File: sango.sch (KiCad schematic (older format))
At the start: 12 parts

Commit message: add high-side driver pFET
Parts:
- added Q?: NTR2101P, Package_TO_SOT_SMD:SOT-23, symbol Transistor_FET:NTR2101P
- added R?: 10k, symbol Device:R
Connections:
- net +5V: now also Q?.2 (S), R?.2
- net at U?.10 (3.0_IND#): now also U?.9 (1.5_IND#), Q?.1 (G), R?.1
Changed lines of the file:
@@
 	1    0    0    -1
 $EndComp
+$Comp
+L Transistor_FET:NTR2101P Q?
+U 1 1 5BE8FFD4
+P 8400 2000
+F 0 "Q?" V 8743 2000 50  0000 C CNN
+F 1 "NTR2101P" V 8652 2000 50  0000 C CNN
+F 2 "Package_TO_SOT_SMD:SOT-23" H 8600 1925 50  0001 L CIN
+F 3 "http://www.onsemi.com/pub/Collateral/NTR2101P-D.PDF" H 8400 2000 50  0001 L CNN
+	1    8400 2000
+	0    1    -1   0
+$EndComp
+Wire Wire Line
+	6800 3150 8400 3150
+Wire Wire Line
+	6800 3300 8400 3300
+Wire Wire Line
+	8400 3300 8400 3150
+Wire Wire Line
+	8400 3150 8400 2400
+Connection ~ 8400 3150
+Wire Wire Line
+	5900 1900 8100 1900
+Connection ~ 5900 1900
+$Comp
+L Device:R R?
+U 1 1 5BE95889
+P 8100 2150
+F 0 "R?" V 8180 2150 50  0000 C CNN
+F 1 "10k" V 8100 2150 50  0000 C CNN
+F 2 "" V 8030 2150 50  0001 C CNN
+F 3 "" H 8100 2150 50  0001 C CNN
+	1    8100 2150
+	-1   0    0    1
+$EndComp
+Wire Wire Line
+	8100 2000 8100 1900
+Connection ~ 8100 1900
+Wire Wire Line
+	8100 1900 8200 1900
+Wire Wire Line
+	8100 2300 8100 2400
+Wire Wire Line
+	8100 2400 8400 2400
+Connection ~ 8400 2400
+Wire Wire Line
+	8400 2400 8400 2200
 $EndSCHEMATC

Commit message: fix: OSC --> OCS typo
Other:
- note added: "TODO: button (to GND) as input to OCS#\nOSC# has a Schmitt-triggered input with a pull-up"
- note removed: "TODO: button (to GND) as input to OSC#\nOSC# has a Schmitt-triggered input with a pull-up"
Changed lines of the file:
@@
 Connection ~ 4350 5100
 Text Notes 4250 1250 0    60   ~ 0
-TODO: button (to GND) as input to OSC#\nOSC# has a Schmitt-triggered input with a pull-up
+TODO: button (to GND) as input to OCS#\nOSC# has a Schmitt-triggered input with a pull-up
 Wire Wire Line
 	4350 3150 4600 3150

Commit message: add Description field to UTC2000 schematic symbol
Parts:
- U?: Description (none) -> Basic USB Type-C Controller; Manufacturer Part Number (none) -> UTC2000-I/MG; ManufacturerPN UTC2000-I/MG -> (none); Supplier (none) -> Digi-Key; Supplier Part Number (none) -> UTC2000-I/MG-ND; Supplier1 Digi-Key -> (none); Supplier1PN UTC2000-I/MG-ND -> (none)
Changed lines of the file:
@@
 F 2 "" H 3900 3400 50  0001 C CIN
 F 3 "http://ww1.microchip.com/downloads/en/DeviceDoc/UTC2000%20DS%2000001957C.pdf" H 5900 2100 50  0001 C CNN
-F 4 "Microchip Technology" H 5900 2100 60  0001 C CNN "Manufacturer"
-F 5 "UTC2000-I/MG" H 5900 2100 60  0001 C CNN "ManufacturerPN"
-F 6 "Digi-Key" H 5900 2100 60  0001 C CNN "Supplier1"
-F 7 "UTC2000-I/MG-ND" H 5900 2100 60  0001 C CNN "Supplier1PN"
+F 4 "Basic USB Type-C Controller" H 5900 2100 60  0001 C CNN "Description"
+F 5 "Microchip Technology" H 5900 2100 60  0001 C CNN "Manufacturer"
+F 6 "UTC2000-I/MG" H 5900 2100 60  0001 C CNN "Manufacturer Part Number"
+F 7 "Digi-Key" H 5900 2100 60  0001 C CNN "Supplier"
+F 8 "UTC2000-I/MG-ND" H 5900 2100 60  0001 C CNN "Supplier Part Number"
 	1    5900 2850
 	1    0    0    -1

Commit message: fix: resistor value for voltage divider on VMON
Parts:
- R?: value 5.1k -> 35.7k
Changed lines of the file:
@@
 P 4200 2550
 F 0 "R?" V 4280 2550 50  0000 C CNN
-F 1 "5.1k" V 4200 2550 50  0000 C CNN
+F 1 "35.7k" V 4200 2550 50  0000 C CNN
 F 2 "" V 4130 2550 50  0001 C CNN
 F 3 "" H 4200 2550 50  0001 C CNN

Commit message: add part numbers for resistors and PFET
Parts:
- Q?: Description (none) -> MOSFET P-CH 8V 3.7A SOT-23; Manufacturer (none) -> ON Semiconductor; Manufacturer Part Number (none) -> NTR2101PT1G; Supplier (none) -> Digi-Key; Supplier Part Number (none) -> NTR2101PT1GOSCT-ND
- R? (x5): Description (none) -> RES SMD 10K OHM 1% 1/10W 0603; Manufacturer (none) -> Panasonic Electronic Components; Manufacturer Part Number (none) -> ERJ-3EKF1002V; Supplier (none) -> Digi-Key; Supplier Part Number (none) -> P10.0KHCT-ND
- R? (x3): Description (none) -> RES SMD 5.1K OHM 1% 1/10W 0603; Manufacturer (none) -> Panasonic Electronic Components; Manufacturer Part Number (none) -> ERJ-3EKF5101V; Supplier (none) -> Digi-Key; Supplier Part Number (none) -> P5.10KHCT-ND
- R?: Description (none) -> RES SMD 35.7K OHM 1% 1/10W 0603; Manufacturer (none) -> Panasonic Electronic Components; Manufacturer Part Number (none) -> ERJ-3EKF3572V; Supplier (none) -> Digi-Key; Supplier Part Number (none) -> P35.7KHCT-ND
- R?: Description (none) -> RES SMD 1M OHM 1% 1/10W 0603; Manufacturer (none) -> Panasonic Electronic Components; Manufacturer Part Number (none) -> ERJ-3EKF1004V; Supplier (none) -> Digi-Key; Supplier Part Number (none) -> P1.00MHCT-ND
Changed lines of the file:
@@
 F 1 "10k" V 4750 3150 50  0000 C CNN
 F 2 "" V 4680 3150 50  0001 C CNN
-F 3 "" H 4750 3150 50  0001 C CNN
+F 3 "https://industrial.panasonic.com/cdbs/www-data/pdf/RDA0000/AOA0000C304.pdf" H 4750 3150 50  0001 C CNN
+F 4 "RES SMD 10K OHM 1% 1/10W 0603" H 4750 3150 50  0001 C CNN "Description"
+F 5 "Panasonic Electronic Components" H 4750 3150 50  0001 C CNN "Manufacturer"
+F 6 "ERJ-3EKF1002V" H 4750 3150 50  0001 C CNN "Manufacturer Part Number"
+F 7 "Digi-Key" H 4750 3150 50  0001 C CNN "Supplier"
+F 8 "P10.0KHCT-ND" H 4750 3150 50  0001 C CNN "Supplier Part Number"
 	1    4750 3150
 	0    -1   -1   0
@@
 F 1 "10k" V 4750 3300 50  0000 C CNN
 F 2 "" V 4680 3300 50  0001 C CNN
-F 3 "" H 4750 3300 50  0001 C CNN
+F 3 "https://industrial.panasonic.com/cdbs/www-data/pdf/RDA0000/AOA0000C304.pdf" H 4750 3300 50  0001 C CNN
+F 4 "RES SMD 10K OHM 1% 1/10W 0603" H 4750 3300 50  0001 C CNN "Description"
+F 5 "Panasonic Electronic Components" H 4750 3300 50  0001 C CNN "Manufacturer"
+F 6 "ERJ-3EKF1002V" H 4750 3300 50  0001 C CNN "Manufacturer Part Number"
+F 7 "Digi-Key" H 4750 3300 50  0001 C CNN "Supplier"
+F 8 "P10.0KHCT-ND" H 4750 3300 50  0001 C CNN "Supplier Part Number"
 	1    4750 3300
 	0    1    1    0
@@
 F 1 "5.1k" V 4500 3550 50  0000 C CNN
 F 2 "" V 4430 3550 50  0001 C CNN
-F 3 "" H 4500 3550 50  0001 C CNN
+F 3 "https://industrial.panasonic.com/cdbs/www-data/pdf/RDA0000/AOA0000C304.pdf" H 4500 3550 50  0001 C CNN
+F 4 "RES SMD 5.1K OHM 1% 1/10W 0603" H 4500 3550 50  0001 C CNN "Description"
+F 5 "Panasonic Electronic Components" H 4500 3550 50  0001 C CNN "Manufacturer"
+F 6 "ERJ-3EKF5101V" H 4500 3550 50  0001 C CNN "Manufacturer Part Number"
+F 7 "Digi-Key" H 4500 3550 50  0001 C CNN "Supplier"
+F 8 "P5.10KHCT-ND" H 4500 3550 50  0001 C CNN "Supplier Part Number"
 	1    4500 3550
 	1    0    0    -1
@@
 F 1 "5.1k" V 4350 3550 50  0000 C CNN
 F 2 "" V 4280 3550 50  0001 C CNN
-F 3 "" H 4350 3550 50  0001 C CNN
+F 3 "https://industrial.panasonic.com/cdbs/www-data/pdf/RDA0000/AOA0000C304.pdf" H 4350 3550 50  0001 C CNN
+F 4 "RES SMD 5.1K OHM 1% 1/10W 0603" H 4350 3550 50  0001 C CNN "Description"
+F 5 "Panasonic Electronic Components" H 4350 3550 50  0001 C CNN "Manufacturer"
+F 6 "ERJ-3EKF5101V" H 4350 3550 50  0001 C CNN "Manufacturer Part Number"
+F 7 "Digi-Key" H 4350 3550 50  0001 C CNN "Supplier"
+F 8 "P5.10KHCT-ND" H 4350 3550 50  0001 C CNN "Supplier Part Number"
 	1    4350 3550
 	-1   0    0    1
@@
 F 1 "10k" V 4700 2150 50  0000 C CNN
 F 2 "" V 4630 2150 50  0001 C CNN
-F 3 "" H 4700 2150 50  0001 C CNN
+F 3 "https://industrial.panasonic.com/cdbs/www-data/pdf/RDA0000/AOA0000C304.pdf" H 4700 2150 50  0001 C CNN
+F 4 "RES SMD 10K OHM 1% 1/10W 0603" H 4700 2150 50  0001 C CNN "Description"
+F 5 "Panasonic Electronic Components" H 4700 2150 50  0001 C CNN "Manufacturer"
+F 6 "ERJ-3EKF1002V" H 4700 2150 50  0001 C CNN "Manufacturer Part Number"
+F 7 "Digi-Key" H 4700 2150 50  0001 C CNN "Supplier"
+F 8 "P10.0KHCT-ND" H 4700 2150 50  0001 C CNN "Supplier Part Number"
 	1    4700 2150
 	-1   0    0    1
@@
 F 1 "10k" V 4850 2150 50  0000 C CNN
 F 2 "" V 4780 2150 50  0001 C CNN
-F 3 "" H 4850 2150 50  0001 C CNN
+F 3 "https://industrial.panasonic.com/cdbs/www-data/pdf/RDA0000/AOA0000C304.pdf" H 4850 2150 50  0001 C CNN
+F 4 "RES SMD 10K OHM 1% 1/10W 0603" H 4850 2150 50  0001 C CNN "Description"
+F 5 "Panasonic Electronic Components" H 4850 2150 50  0001 C CNN "Manufacturer"
+F 6 "ERJ-3EKF1002V" H 4850 2150 50  0001 C CNN "Manufacturer Part Number"
+F 7 "Digi-Key" H 4850 2150 50  0001 C CNN "Supplier"
+F 8 "P10.0KHCT-ND" H 4850 2150 50  0001 C CNN "Supplier Part Number"
 	1    4850 2150
 	1    0    0    -1
@@
 F 1 "5.1k" V 4200 2950 50  0000 C CNN
 F 2 "" V 4130 2950 50  0001 C CNN
-F 3 "" H 4200 2950 50  0001 C CNN
+F 3 "https://industrial.panasonic.com/cdbs/www-data/pdf/RDA0000/AOA0000C304.pdf" H 4200 2950 50  0001 C CNN
+F 4 "RES SMD 5.1K OHM 1% 1/10W 0603" H 4200 2950 50  0001 C CNN "Description"
+F 5 "Panasonic Electronic Components" H 4200 2950 50  0001 C CNN "Manufacturer"
+F 6 "ERJ-3EKF5101V" H 4200 2950 50  0001 C CNN "Manufacturer Part Number"
+F 7 "Digi-Key" H 4200 2950 50  0001 C CNN "Supplier"
+F 8 "P5.10KHCT-ND" H 4200 2950 50  0001 C CNN "Supplier Part Number"
 	1    4200 2950
 	-1   0    0    1
@@
 F 1 "35.7k" V 4200 2550 50  0000 C CNN
 F 2 "" V 4130 2550 50  0001 C CNN
-F 3 "" H 4200 2550 50  0001 C CNN
+F 3 "https://industrial.panasonic.com/cdbs/www-data/pdf/RDA0000/AOA0000C304.pdf" H 4200 2550 50  0001 C CNN
+F 4 "RES SMD 35.7K OHM 1% 1/10W 0603" H 4200 2550 50  0001 C CNN "Description"
+F 5 "Panasonic Electronic Components" H 4200 2550 50  0001 C CNN "Manufacturer"
+F 6 "ERJ-3EKF3572V" H 4200 2550 50  0001 C CNN "Manufacturer Part Number"
+F 7 "Digi-Key" H 4200 2550 50  0001 C CNN "Supplier"
+F 8 "P35.7KHCT-ND" H 4200 2550 50  0001 C CNN "Supplier Part Number"
 	1    4200 2550
 	-1   0    0    1
@@
 F 1 "1M" V 2900 4850 50  0000 C CNN
 F 2 "" V 2830 4850 50  0001 C CNN
-F 3 "" H 2900 4850 50  0001 C CNN
+F 3 "https://industrial.panasonic.com/cdbs/www-data/pdf/RDA0000/AOA0000C304.pdf" H 2900 4850 50  0001 C CNN
+F 4 "RES SMD 1M OHM 1% 1/10W 0603" H 2900 4850 50  0001 C CNN "Description"
+F 5 "Panasonic Electronic Components" H 2900 4850 50  0001 C CNN "Manufacturer"
+F 6 "ERJ-3EKF1004V" H 2900 4850 50  0001 C CNN "Manufacturer Part Number"
+F 7 "Digi-Key" H 2900 4850 50  0001 C CNN "Supplier"
+F 8 "P1.00MHCT-ND" H 2900 4850 50  0001 C CNN "Supplier Part Number"
 	1    2900 4850
 	1    0    0    1
@@
 F 2 "Package_TO_SOT_SMD:SOT-23" H 8600 1925 50  0001 L CIN
 F 3 "http://www.onsemi.com/pub/Collateral/NTR2101P-D.PDF" H 8400 2000 50  0001 L CNN
+F 4 "MOSFET P-CH 8V 3.7A SOT-23" H 8400 2000 50  0001 L CNN "Description"
+F 5 "ON Semiconductor" H 8400 2000 50  0001 L CNN "Manufacturer"
+F 6 "NTR2101PT1G" H 8400 2000 50  0001 L CNN "Manufacturer Part Number"
+F 7 "Digi-Key" H 8400 2000 50  0001 L CNN "Supplier"
+F 8 "NTR2101PT1GOSCT-ND" H 8400 2000 50  0001 L CNN "Supplier Part Number"
 	1    8400 2000
 	0    1    -1   0
@@
 F 1 "10k" V 8100 2150 50  0000 C CNN
 F 2 "" V 8030 2150 50  0001 C CNN
-F 3 "" H 8100 2150 50  0001 C CNN
+F 3 "https://industrial.panasonic.com/cdbs/www-data/pdf/RDA0000/AOA0000C304.pdf" H 8100 2150 50  0001 C CNN
+F 4 "RES SMD 10K OHM 1% 1/10W 0603" H 8100 2150 50  0001 C CNN "Description"
+F 5 "Panasonic Electronic Components" H 8100 2150 50  0001 C CNN "Manufacturer"
+F 6 "ERJ-3EKF1002V" H 8100 2150 50  0001 C CNN "Manufacturer Part Number"
+F 7 "Digi-Key" H 8100 2150 50  0001 C CNN "Supplier"
+F 8 "P10.0KHCT-ND" H 8100 2150 50  0001 C CNN "Supplier Part Number"
 	1    8100 2150
 	-1   0    0    1

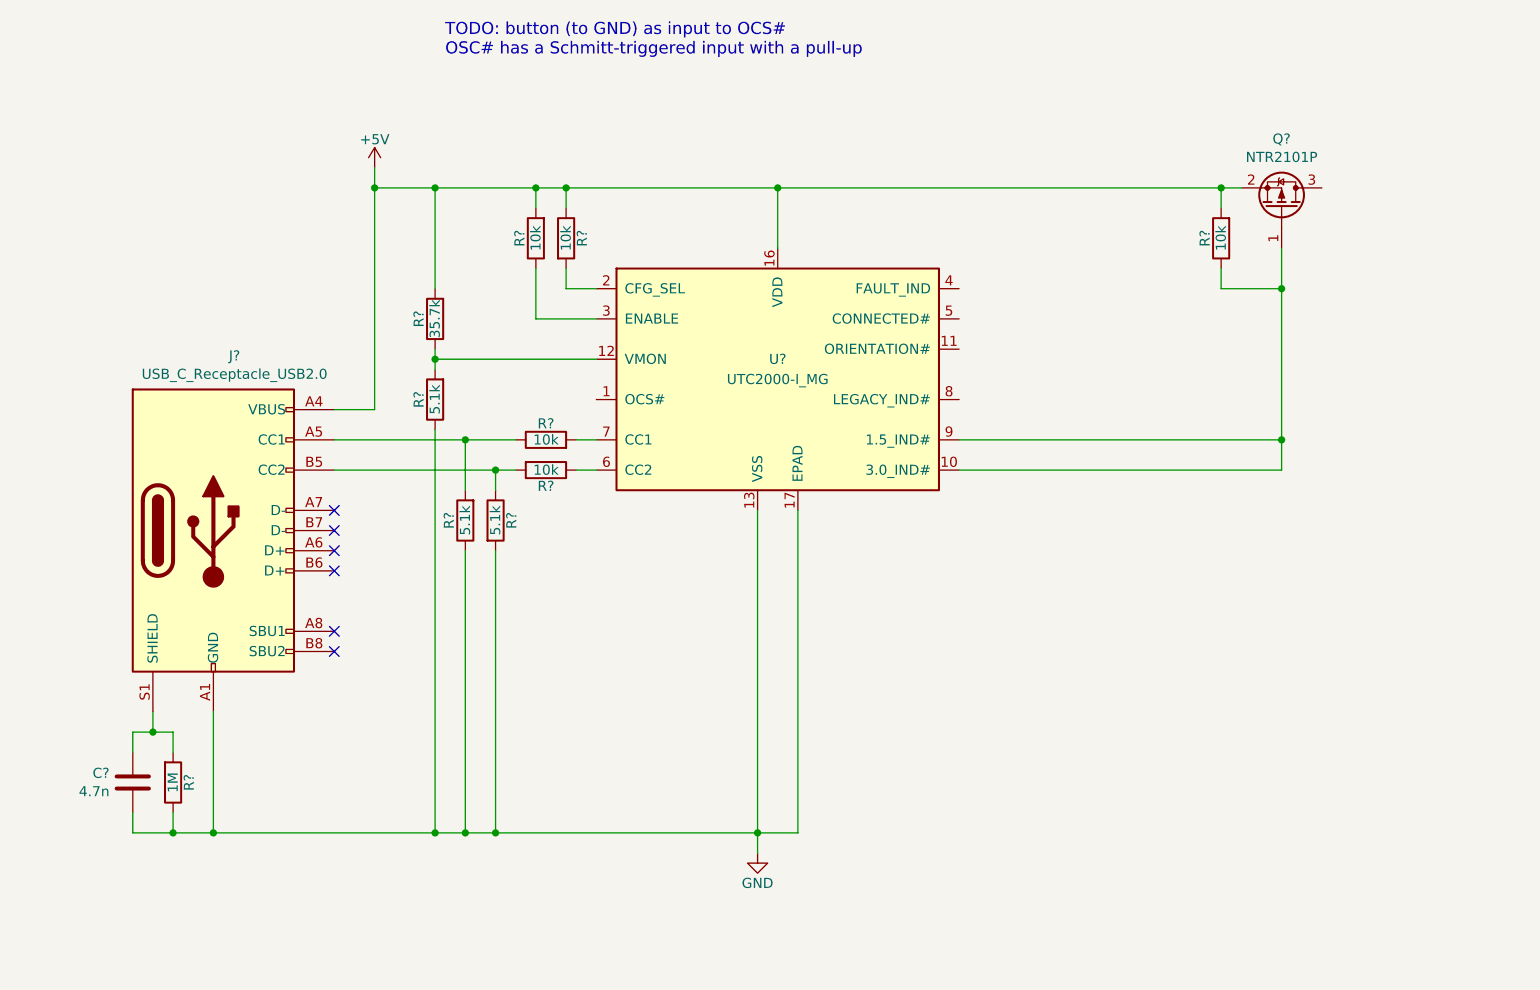
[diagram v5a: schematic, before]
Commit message: add LEDs and testpads, re-center
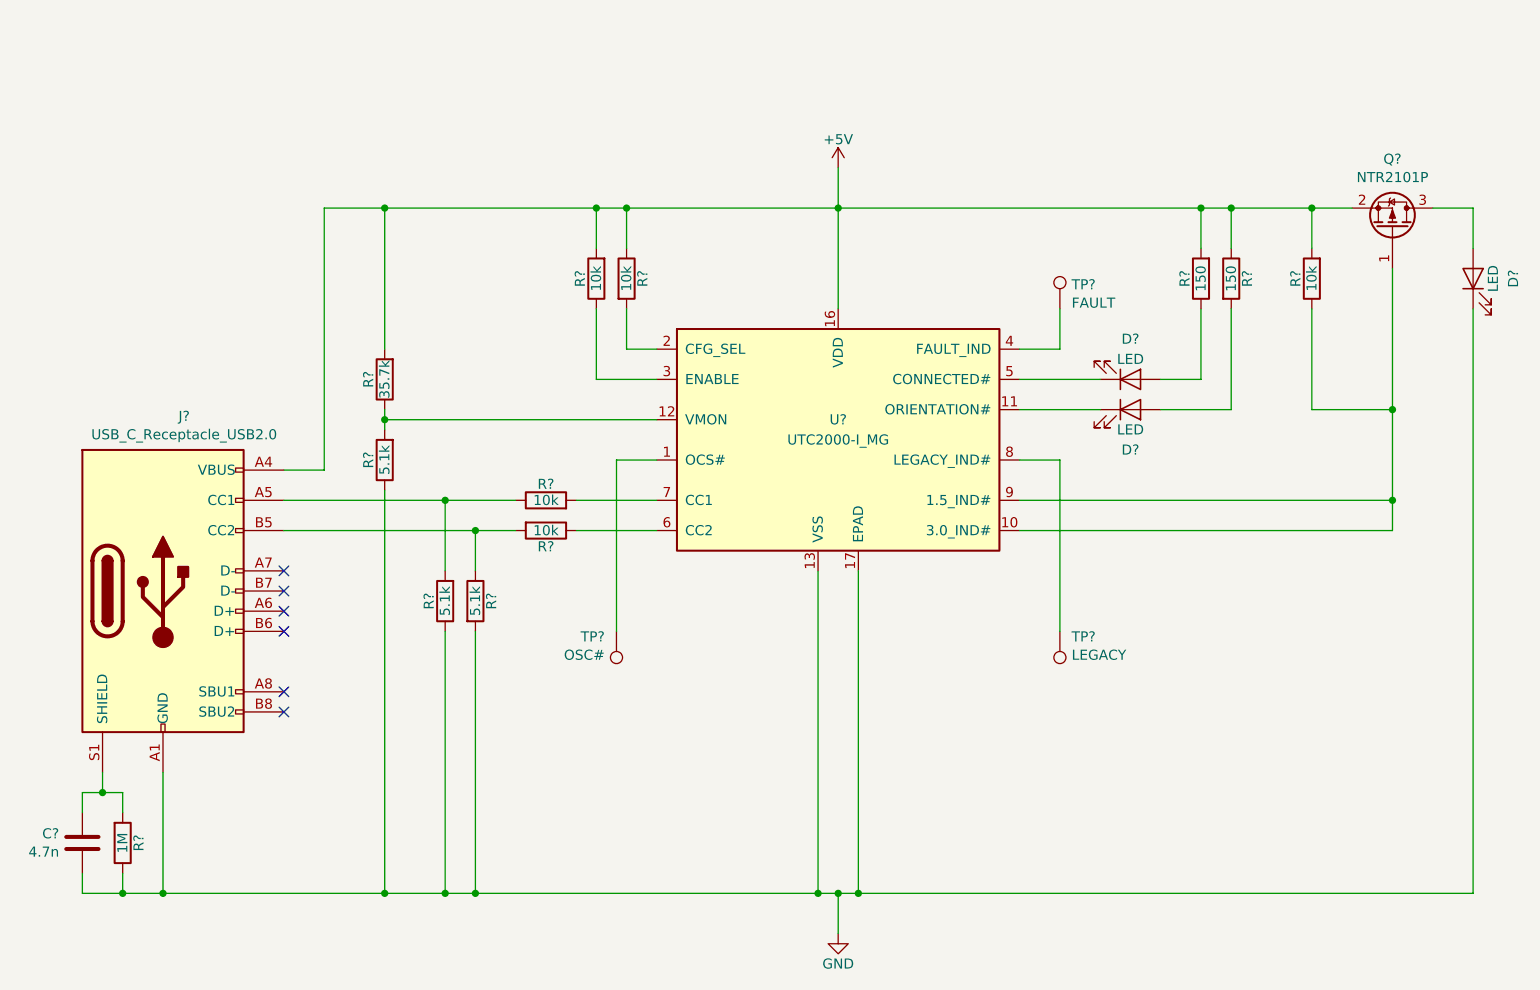
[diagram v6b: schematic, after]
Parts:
- added D? (x3): LED, symbol Device:LED
- added R? (x2): 150, symbol Device:R
- added TP?: OSC#, symbol Connector:TestPoint
- added TP?: LEGACY, symbol Connector:TestPoint
- added TP?: FAULT, symbol Connector:TestPoint
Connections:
- net +5V: now also R?.1, R?.2
- net GND: now also D?.1 (K)
- net at U?.1 (OCS#): now also TP?.1
- net at U?.11 (ORIENTATION#): now also D?.1 (K)
- net at U?.4 (FAULT_IND): now also TP?.1
- net at U?.5 (CONNECTED#): now also D?.1 (K)
- net at U?.8 (LEGACY_IND#): now also TP?.1
- net at Q?.3 (D): now also D?.2 (A)
- new net: D?.2 (A), R?.2
- new net: D?.2 (A), R?.1
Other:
- note removed: "TODO: button (to GND) as input to OCS#\nOSC# has a Schmitt-triggered input with a pull-up"
- moved on the sheet: C?, J?, Q?, R?, U?
